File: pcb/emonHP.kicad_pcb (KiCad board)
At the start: 4 copper layers, 85 x 88 mm, 107 parts, among them CN1 CONN_03SCREW, CN3 Screw_Terminal_01x02, CN4 CONN_03SCREW, CN5 Screw_Terminal_01x02, J1 CONN_04PTH, J2 CONN_04PTH, J3 USB_C_Receptacle_USB2.0, J4 Conn_ARM_JTAG_SWD_10, J5 Conn_02x20_Odd_Even, Q1 Q_NPN_BEC_BRT, Q2 FDN5618P, Q3 Q_NPN_BEC_BRT, SW1 SW_Push, SW2 SW_Push, U1 HCPL-3700M, U10 SN74LVC1T45DRL, U2 ATSAMD21G15B-A, U3 AP2112K-3.3, U4 RFM69CW, U5 LM2733XMF, U6 LM4040DBZ-5, U7 MC33072, U8 THVD1400D, U9 USBLC6-2P6

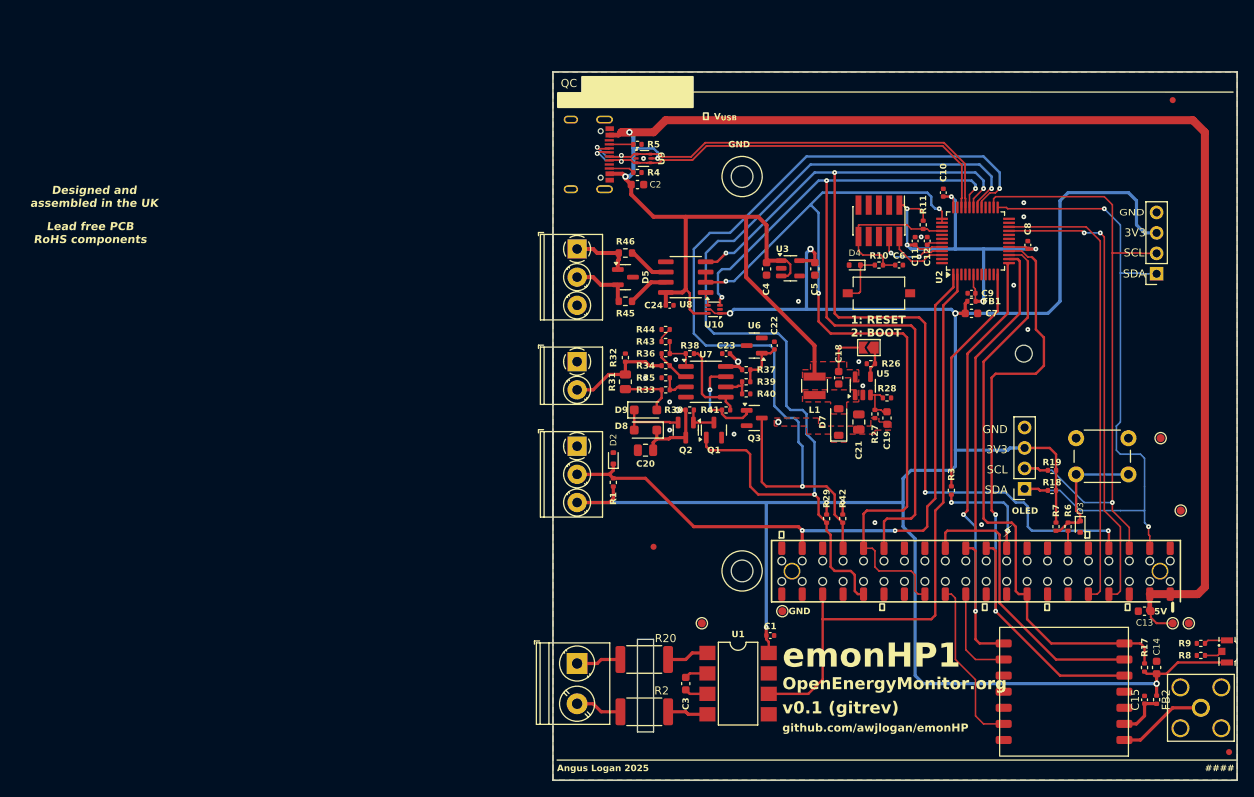
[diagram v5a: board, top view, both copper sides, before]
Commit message: Move SAMD below, reroute
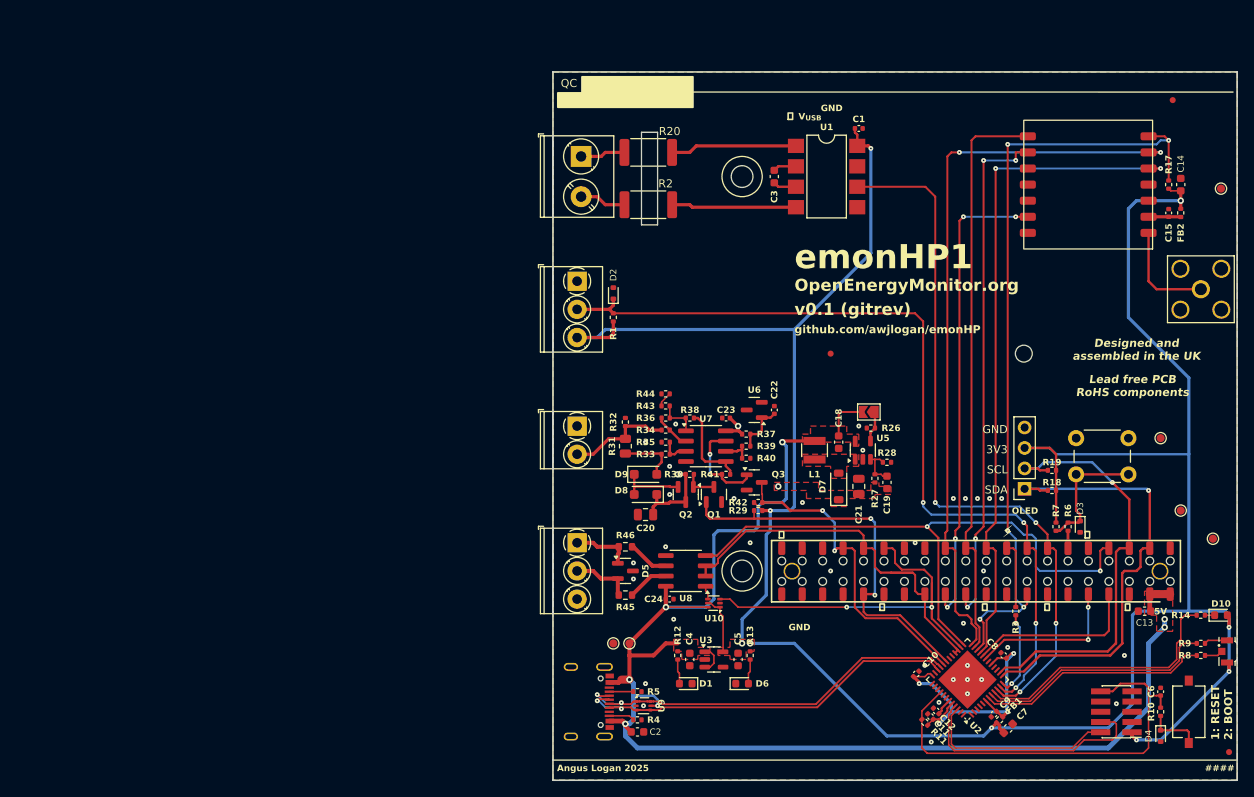
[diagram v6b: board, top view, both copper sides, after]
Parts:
- removed J1: CONN_04PTH, Connector_PinSocket_2.54mm:PinSocket_1x04_P2.54mm_Vertical
- added D1: LED, LED_SMD:LED_0603_1608Metric, F.Cu at (121.5, 138.0)
- added D10: LED, LED_SMD:LED_0603_1608Metric, F.Cu at (188.0, 129.5)
- added D6: LED, LED_SMD:LED_0603_1608Metric, F.Cu at (128.5, 138.0)
- added R12: 1K, Resistor_SMD:R_0402_1005Metric, F.Cu at (120.5, 134.5)
- added R13: 1K, Resistor_SMD:R_0402_1005Metric, F.Cu at (129.5, 134.5)
- added R14: 1K, Resistor_SMD:R_0402_1005Metric, F.Cu at (185.5, 129.5)
- U2: value ATSAMD21G15B-A -> ATSAMD21G15B-M; footprint Package_QFP:TQFP-48_7x7mm_P0.5mm -> Package_DFN_QFN:QFN-48-1EP_7x7mm_P0.5mm_EP5.15x5.15mm
- moved TP7 84.1 mm to (188.0, 76.5)
- moved D4 69.8 mm to (180.5, 144.5), turned to -90 degrees
- moved C2 68.0 mm to (115.5, 144.0)
- moved J3 68.0 mm to (108.5, 140.5)
- moved R4 68.0 mm to (115.5, 142.5)
- moved R5 68.0 mm to (115.5, 139.0)
- moved U9 68.0 mm to (116.2, 140.8)
- moved J4 67.8 mm to (175.0, 141.5), turned to 180 degrees
- moved TP1 67.5 mm to (114.5, 133.0)
- moved R10 65.6 mm to (180.5, 141.5), turned to 90 degrees
- moved SW2 64.7 mm to (184.0, 141.5), turned to 90 degrees
- moved C1 64.0 mm to (143.0, 69.0)
- moved C3 64.0 mm to (132.5, 75.0)
- moved U1 64.0 mm to (139.0, 75.0)
- moved U4 63.1 mm to (171.5, 76.0)
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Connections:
- J4 pad 1: /Vuc -> +3V3
- J5 pad 13: unconnected-(J5-Pin_13-Pad13) -> /DHW_SENSE
- J5 pad 15: unconnected-(J5-Pin_15-Pad15) -> /OPA1
- J5 pad 25: unconnected-(J5-Pin_25-Pad25) -> GND
- J5 pad 36: /DHW_SENSE -> unconnected-(J5-Pin_36-Pad36)
- J5 pad 37: /OPA1 -> unconnected-(J5-Pin_37-Pad37)
- U2 pad 1: /OPA1 -> unconnected-(U2-PA00-Pad1)
- U2 pad 10: unconnected-(U2-PA05-Pad10) -> /DHW_SENSE
- U2 pad 11: unconnected-(U2-PA06-Pad11) -> /OPA1
- U2 pad 13: /RFM_MISO -> /I2C_SDA
- U2 pad 14: /RFM_SCK -> /I2C_SCL
- U2 pad 15: /RFM_SEL -> unconnected-(U2-PA10-Pad15)
- U2 pad 16: /RFM_MOSI -> unconnected-(U2-PA11-Pad16)
- U2 pad 19: unconnected-(U2-PB10-Pad19) -> /UART0_TX
- U2 pad 2: /DHW_SENSE -> unconnected-(U2-PA01-Pad2)
- U2 pad 20: unconnected-(U2-PB11-Pad20) -> /UART0_RX
- U2 pad 21: /UART0_RX -> /RFM_MOSI
- U2 pad 22: /UART0_TX -> /RFM_SEL
- U2 pad 23: unconnected-(U2-PA14-Pad23) -> /RFM_MISO
- U2 pad 24: unconnected-(U2-PA15-Pad24) -> /RFM_SCK
- U2 pad 25: /I2C_SDA -> /UART3_TX
- U2 pad 26: /I2C_SCL -> /UART3_RX
- U2 pad 27: unconnected-(U2-PA18-Pad27) -> /UART3_RTS
- U2 pad 28: unconnected-(U2-PA19-Pad28) -> /UART3_RTS
- U2 pad 29: /UART5_RX -> unconnected-(U2-PA20-Pad29)
- U2 pad 30: /UART5_TX -> unconnected-(U2-PA21-Pad30)
- U2 pad 31: /UART3_TX -> /UART5_TX
- U2 pad 32: /UART3_RX -> /UART5_RX
- U2 pad 37: /UART3_RTS -> unconnected-(U2-PB22-Pad37)
- U2 pad 38: /UART3_RTS -> unconnected-(U2-PB23-Pad38)
- U2 pad 7: unconnected-(U2-PB08-Pad7) -> /~{LED_STATUS}
- U2 pad 8: unconnected-(U2-PB09-Pad8) -> /~{LED_PROG}
- U2 pad 9: unconnected-(U2-PA04-Pad9) -> /~{LED_ACT}
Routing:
- net /UART5_RX: track 114.3 -> 39.8 mm
- net /UART5_TX: track 122.3 -> 49.5 mm
- net +5V: track 238.1 -> 175.5 mm, vias 3 -> 7
- net /UART3_RTS: track 108.3 -> 50.3 mm, vias 3 -> 0
- net /UART3_RX: track 103.6 -> 50.3 mm, vias 3 -> 2
- net /RFM_IRQ: track 12.1 -> 64.5 mm, vias 0 -> 4
- net +3V3: track 273.4 -> 320.0 mm, vias 7 -> 9
- net /UART3_TX: track 122.0 -> 75.5 mm, vias 5 -> 2
- net /RFM_RESET: track 21.0 -> 59.1 mm, vias 0 -> 4
- net /UART0_TX: track 57.2 -> 19.4 mm, vias 0 -> 2
- net /UART0_RX: track 58.6 -> 21.5 mm, vias 2 -> 0
- net /~{RESET}: track 19.8 -> 53.7 mm
- net /~{LED_ACT}: track 0.00 -> 32.4 mm
- net /~{LED_PROG}: track 0.00 -> 29.8 mm
- net /~{LED_STATUS}: track 0.00 -> 28.9 mm
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- added copper zone on F.Cu, net +3V3
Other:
- outline, holes or cut-outs redrawn

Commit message: Swap 1Wire and AC sense
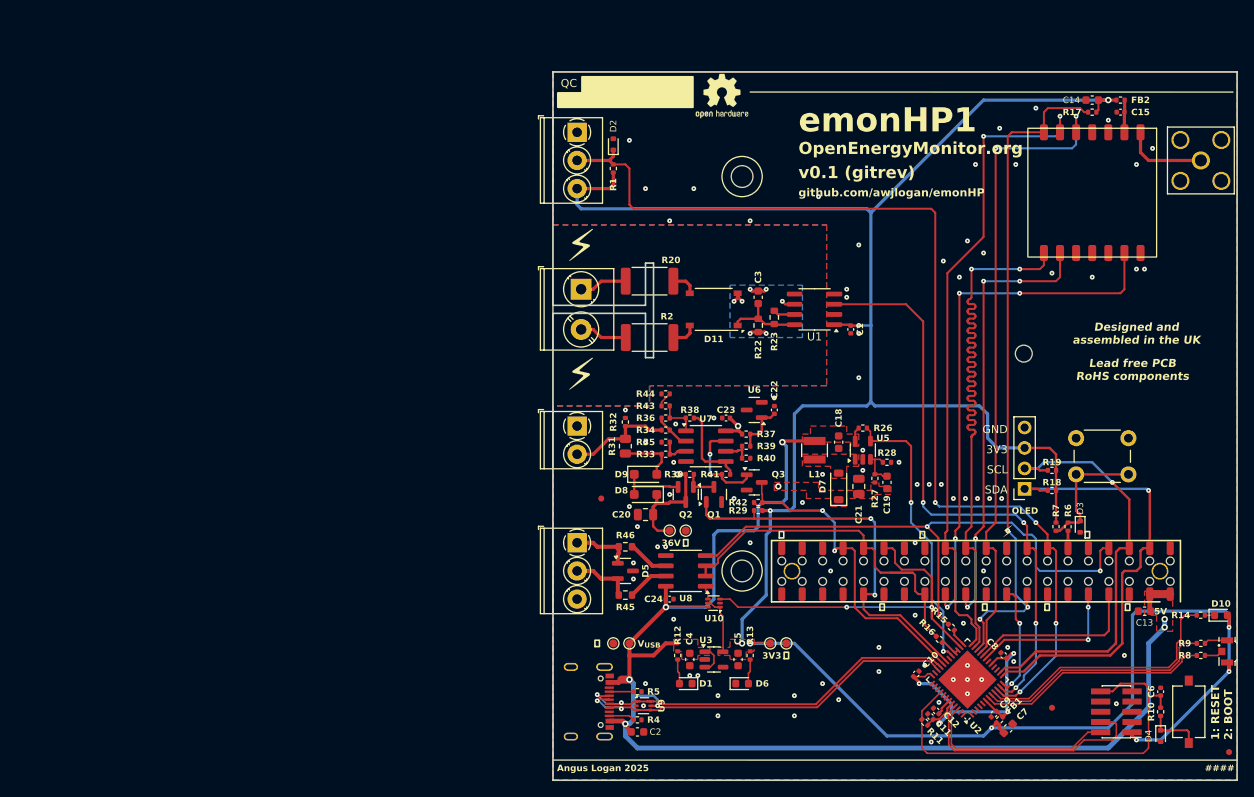
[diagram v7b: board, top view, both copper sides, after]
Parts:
- removed JP1: Jumper_2_Open, Jumper:SolderJumper-2_P1.3mm_Open_TrianglePad1.0x1.5mm
- removed R3: 1K, Resistor_SMD:R_0402_1005Metric
- removed TP7, TP8: TestPoint, TestPoint:TestPoint_Pad_D1.0mm
- added D11: ABS6, Diode_SMD:Diode_Bridge_Diotec_ABS, F.Cu at (125.0, 91.5)
- added R15: 1K, Resistor_SMD:R_0402_1005Metric, F.Cu at (154.5, 131.0)
- added R16: 1K, Resistor_SMD:R_0402_1005Metric, F.Cu at (153.0, 132.5)
- added R22: 15K, Resistor_SMD:R_0603_1608Metric, F.Cu at (130.5, 93.5)
- added R23: 560, Resistor_SMD:R_0603_1608Metric, F.Cu at (132.5, 92.5)
- added REF**: OSHW-Logo2_7.3x6mm_SilkScreen, Symbol:OSHW-Logo2_7.3x6mm_SilkScreen, F.Cu at (126.0, 65.0)
- added TP2: TestPoint, TestPoint:TestPoint_Pad_D1.0mm, F.Cu at (132.0, 133.0)
- added TP3: TestPoint, TestPoint:TestPoint_Pad_D1.0mm, F.Cu at (119.5, 119.0)
- D7: value MBR0550 -> MBR0580
- R17, R26: value 47K -> 100K
- R18, R19: value 4K7 -> 5K1
- R2, R20: value 37.4K -> 30K
- U1: value HCPL-3700M -> ISO1211; footprint Package_DIP:SMDIP-8_W7.62mm -> Package_SO:SOIC-8_3.9x4.9mm_P1.27mm
- moved FD3 77.0 mm to (167.0, 141.0)
- moved TP4 61.6 mm to (121.5, 119.0)
- moved TP6 54.6 mm to (134.0, 133.0)
- moved FD1 33.7 mm to (111.0, 115.0)
- moved C1 25.0 mm to (142.0, 94.0), turned to -90 degrees
- moved CN1 18.5 mm to (108.0, 69.5)
- moved D2 18.5 mm to (112.5, 71.0)
- moved R1 18.5 mm to (112.5, 74.0)
- moved U1 16.6 mm to (137.5, 91.5), turned to 180 degrees
- moved R2 16.5 mm to (117.0, 95.0)
- moved CN5 16.5 mm to (108.5, 89.0)
- moved R20 16.0 mm to (117.0, 88.0)
- moved SMA1 16.0 mm to (185.5, 73.0)
- moved FB2 15.9 mm to (175.5, 65.5), turned to 0 degrees
- moved C14 15.2 mm to (172.0, 65.5), turned to 180 degrees
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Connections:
- C3 pad 1: Net-(U1-DC+) -> Net-(D11-+)
- C3 pad 2: Net-(U1-DC-) -> GND1
- J5 pad 13: /DHW_SENSE -> /OPA1
- J5 pad 15: /OPA1 -> /DHW_SENSE
- J5 pad 17: /PI_3V3 -> unconnected-(J5-Pin_17-Pad17)
- J5 pad 18: unconnected-(J5-Pin_18-Pad18) -> /~{PI_PRESENT}
- R2 pad 2: Net-(U1-AC1) -> Net-(D11-Pad4)
- R20 pad 2: Net-(U1-AC0) -> Net-(D11-Pad3)
- R26 pad 1: /MBUS_EN -> +5V
- R26 pad 2: GND -> /MBUS_EN
- U1 pad 1: Net-(U1-AC0) -> +3V3
- U1 pad 2: Net-(U1-DC+) -> unconnected-(U1-EN-Pad2)
- U1 pad 3: Net-(U1-DC-) -> /DHW_SENSE
- U1 pad 4: Net-(U1-AC1) -> GND
- U1 pad 5: GND -> unconnected-(U1-SUB-Pad5)
- U1 pad 6: /DHW_SENSE -> GND1
- U1 pad 7: (no net) -> Net-(U1-IN)
- U1 pad 8: +3V3 -> Net-(D11-+)
- U2 pad 10: /DHW_SENSE -> /OPA1
- U2 pad 11: /OPA1 -> /DHW_SENSE
- U2 pad 12: Net-(U2-PA07) -> /~{PI_PRESENT}
- U2 pad 25: /UART3_TX -> /UART3_TX_uc
- U2 pad 27: /UART3_RTS -> /UART3_RTS_uc
- U2 pad 28: /UART3_RTS -> /UART3_RTS_uc
- U2 pad 29: unconnected-(U2-PA20-Pad29) -> /MBUS_EN
- U2 pad 39: unconnected-(U2-PA27-Pad39) -> GND
- U2 pad 41: unconnected-(U2-PA28-Pad41) -> GND
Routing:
- net /MBUS_EN: track 3.81 -> 35.6 mm, vias 0 -> 2
- net /OPA1: track 106.5 -> 128.6 mm
- net /DHW_SENSE: track 89.5 -> 73.3 mm
- net Net-(U1-AC0): track 15.7 -> 0.00 mm
- net Net-(U1-AC1): track 15.5 -> 0.00 mm
- net /~{PI_PRESENT}: track 0.00 -> 14.2 mm, vias 0 -> 2
- net /RFM_SEL: track 98.5 -> 85.2 mm, vias 5 -> 3
- net +3V3: track 320.0 -> 308.8 mm
- net Net-(U2-PA07): track 10.7 -> 0.00 mm, vias 2 -> 0
- net /RFM_SCK: track 91.9 -> 81.8 mm
- net Net-(D11-+): track 0.00 -> 9.59 mm
- net /RFM_IRQ: track 64.5 -> 55.7 mm
- net GND1: track 0.00 -> 8.42 mm, vias 0 -> 7
- net /PI_3V3: track 8.25 -> 0.00 mm
- net /RFM_MISO: track 72.0 -> 80.1 mm, vias 0 -> 2
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- added copper zone on B.Cu, net GND1
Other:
- outline, holes or cut-outs redrawn
- board text added: "36V"
